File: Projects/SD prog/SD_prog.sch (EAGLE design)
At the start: 2 parts

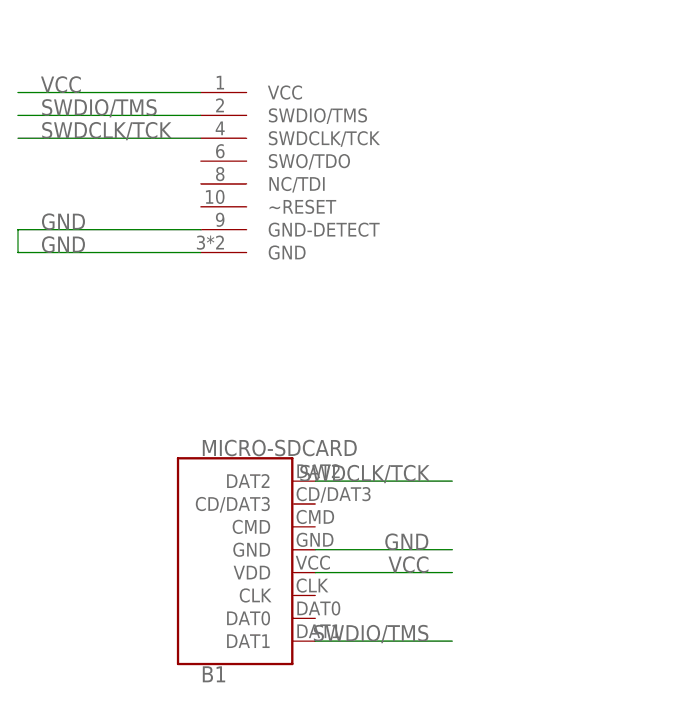
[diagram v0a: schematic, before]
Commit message: Added buttons on ZLL Added pads on nRF51 key SD prog finished N5 lib updated
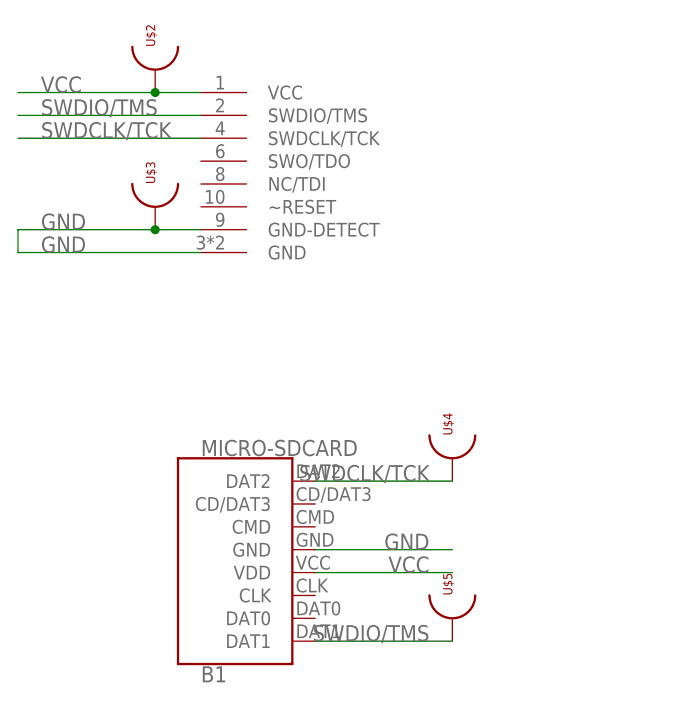
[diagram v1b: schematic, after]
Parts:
- added U$2, U$3, U$4, U$5: TESTPOINT_33, test_points:TESTPOINT_33
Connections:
- net GND: now also U$3.P$1
- net SWDCLK/TCK: now also U$4.P$1
- net SWDIO/TMS: now also U$5.P$1
- net VCC: now also U$2.P$1
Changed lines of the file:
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@@
 <part name="B1" library="SD_Card" deviceset="MICRO-SDCARD" device=""/>
 <part name="U$1" library="con-cortex" deviceset="2X5_0.05&quot;_CORTEX_DEBUG" device="TH_NOKEY_UNSHROUDED"/>
+<part name="U$2" library="test_points" deviceset="TESTPOINT_33" device=""/>
+<part name="U$3" library="test_points" deviceset="TESTPOINT_33" device=""/>
+<part name="U$4" library="test_points" deviceset="TESTPOINT_33" device=""/>
+<part name="U$5" library="test_points" deviceset="TESTPOINT_33" device=""/>
 </parts>
 <sheets>
@@
 </instance>
 <instance part="U$1" gate="G$1" x="7.62" y="86.36" smashed="yes"/>
+<instance part="U$2" gate="G$1" x="0" y="96.52" smashed="yes">
+<attribute name="NAME" x="0" y="101.6" size="1.016" layer="94" rot="R90"/>
+</instance>
+<instance part="U$3" gate="G$1" x="0" y="81.28" smashed="yes">
+<attribute name="NAME" x="0" y="86.36" size="1.016" layer="94" rot="R90"/>
+</instance>
+<instance part="U$4" gate="G$1" x="33.02" y="53.34" smashed="yes">
+<attribute name="NAME" x="33.02" y="58.42" size="1.016" layer="94" rot="R90"/>
+</instance>
+<instance part="U$5" gate="G$1" x="33.02" y="35.56" smashed="yes">
+<attribute name="NAME" x="33.02" y="40.64" size="1.016" layer="94" rot="R90"/>
+</instance>
 </instances>
 <busses>
@@
 <segment>
 <pinref part="U$1" gate="G$1" pin="VCC"/>
-<wire x1="5.08" y1="96.52" x2="-15.24" y2="96.52" width="0.1524" layer="91"/>
+<wire x1="5.08" y1="96.52" x2="0" y2="96.52" width="0.1524" layer="91"/>
 <label x="-12.7" y="96.52" size="1.778" layer="95"/>
+<pinref part="U$2" gate="G$1" pin="P$1"/>
+<wire x1="0" y1="96.52" x2="-15.24" y2="96.52" width="0.1524" layer="91"/>
+<junction x="0" y="96.52"/>
 </segment>
 <segment>
@@
 <wire x1="17.78" y1="35.56" x2="33.02" y2="35.56" width="0.1524" layer="91"/>
 <label x="30.48" y="35.56" size="1.778" layer="95" align="bottom-right"/>
+<pinref part="U$5" gate="G$1" pin="P$1"/>
 </segment>
 </net>
@@
 <wire x1="17.78" y1="53.34" x2="33.02" y2="53.34" width="0.1524" layer="91"/>
 <label x="30.48" y="53.34" size="1.778" layer="95" align="bottom-right"/>
+<pinref part="U$4" gate="G$1" pin="P$1"/>
 </segment>
 </net>
@@
 <label x="-12.7" y="78.74" size="1.778" layer="95"/>
 <pinref part="U$1" gate="G$1" pin="GND-DETECT"/>
-<wire x1="5.08" y1="81.28" x2="-15.24" y2="81.28" width="0.1524" layer="91"/>
+<wire x1="5.08" y1="81.28" x2="0" y2="81.28" width="0.1524" layer="91"/>
 <label x="-12.7" y="81.28" size="1.778" layer="95"/>
+<wire x1="0" y1="81.28" x2="-15.24" y2="81.28" width="0.1524" layer="91"/>
 <wire x1="-15.24" y1="78.74" x2="-15.24" y2="81.28" width="0.1524" layer="91"/>
+<pinref part="U$3" gate="G$1" pin="P$1"/>
+<junction x="0" y="81.28"/>
 </segment>
 <segment>

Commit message: Order @ Boktech
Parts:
- added U$6, U$7, U$8, U$9: TESTPOINT_22, test_points:TESTPOINT_22
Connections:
- new net N$1: B1.CD/DAT3, U$6.P$1
- new net N$2: B1.CMD, U$7.P$1
- new net N$3: B1.CLK, U$8.P$1
- new net N$4: B1.DAT0, U$9.P$1
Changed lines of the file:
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@@
 <part name="U$4" library="test_points" deviceset="TESTPOINT_33" device=""/>
 <part name="U$5" library="test_points" deviceset="TESTPOINT_33" device=""/>
+<part name="U$6" library="test_points" deviceset="TESTPOINT_22" device=""/>
+<part name="U$7" library="test_points" deviceset="TESTPOINT_22" device=""/>
+<part name="U$8" library="test_points" deviceset="TESTPOINT_22" device=""/>
+<part name="U$9" library="test_points" deviceset="TESTPOINT_22" device=""/>
 </parts>
 <sheets>
@@
 <instance part="U$5" gate="G$1" x="33.02" y="35.56" smashed="yes">
 <attribute name="NAME" x="33.02" y="40.64" size="1.016" layer="94" rot="R90"/>
+</instance>
+<instance part="U$6" gate="G$1" x="45.72" y="50.8" smashed="yes">
+<attribute name="NAME" x="45.72" y="55.88" size="1.016" layer="94" rot="R90"/>
+</instance>
+<instance part="U$7" gate="G$1" x="45.72" y="48.26" smashed="yes" rot="R180">
+<attribute name="NAME" x="45.72" y="43.18" size="1.016" layer="94" rot="R270"/>
+</instance>
+<instance part="U$8" gate="G$1" x="53.34" y="40.64" smashed="yes">
+<attribute name="NAME" x="53.34" y="45.72" size="1.016" layer="94" rot="R90"/>
+</instance>
+<instance part="U$9" gate="G$1" x="53.34" y="38.1" smashed="yes" rot="R180">
+<attribute name="NAME" x="53.34" y="33.02" size="1.016" layer="94" rot="R270"/>
 </instance>
 </instances>
@@
 </segment>
 </net>
+<net name="N$1" class="0">
+<segment>
+<pinref part="B1" gate="G$1" pin="CD/DAT3"/>
+<pinref part="U$6" gate="G$1" pin="P$1"/>
+<wire x1="17.78" y1="50.8" x2="45.72" y2="50.8" width="0.1524" layer="91"/>
+</segment>
+</net>
+<net name="N$2" class="0">
+<segment>
+<pinref part="B1" gate="G$1" pin="CMD"/>
+<pinref part="U$7" gate="G$1" pin="P$1"/>
+<wire x1="17.78" y1="48.26" x2="45.72" y2="48.26" width="0.1524" layer="91"/>
+</segment>
+</net>
+<net name="N$3" class="0">
+<segment>
+<pinref part="U$8" gate="G$1" pin="P$1"/>
+<pinref part="B1" gate="G$1" pin="CLK"/>
+<wire x1="53.34" y1="40.64" x2="17.78" y2="40.64" width="0.1524" layer="91"/>
+</segment>
+</net>
+<net name="N$4" class="0">
+<segment>
+<pinref part="B1" gate="G$1" pin="DAT0"/>
+<pinref part="U$9" gate="G$1" pin="P$1"/>
+<wire x1="17.78" y1="38.1" x2="53.34" y2="38.1" width="0.1524" layer="91"/>
+</segment>
+</net>
